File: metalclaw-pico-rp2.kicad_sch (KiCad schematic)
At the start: 114 parts, among them J1 USB_C_Receptacle_USB2.0_14P, J2 Conn_02x05_Odd_Even, SW1 SW_Push, SW2 SW_Push, U1 XC6220B331MR, U2 RP2354B, U3 APS6404L-3SQRx-SN, Y1 XRCGB40M000F1S2FR0

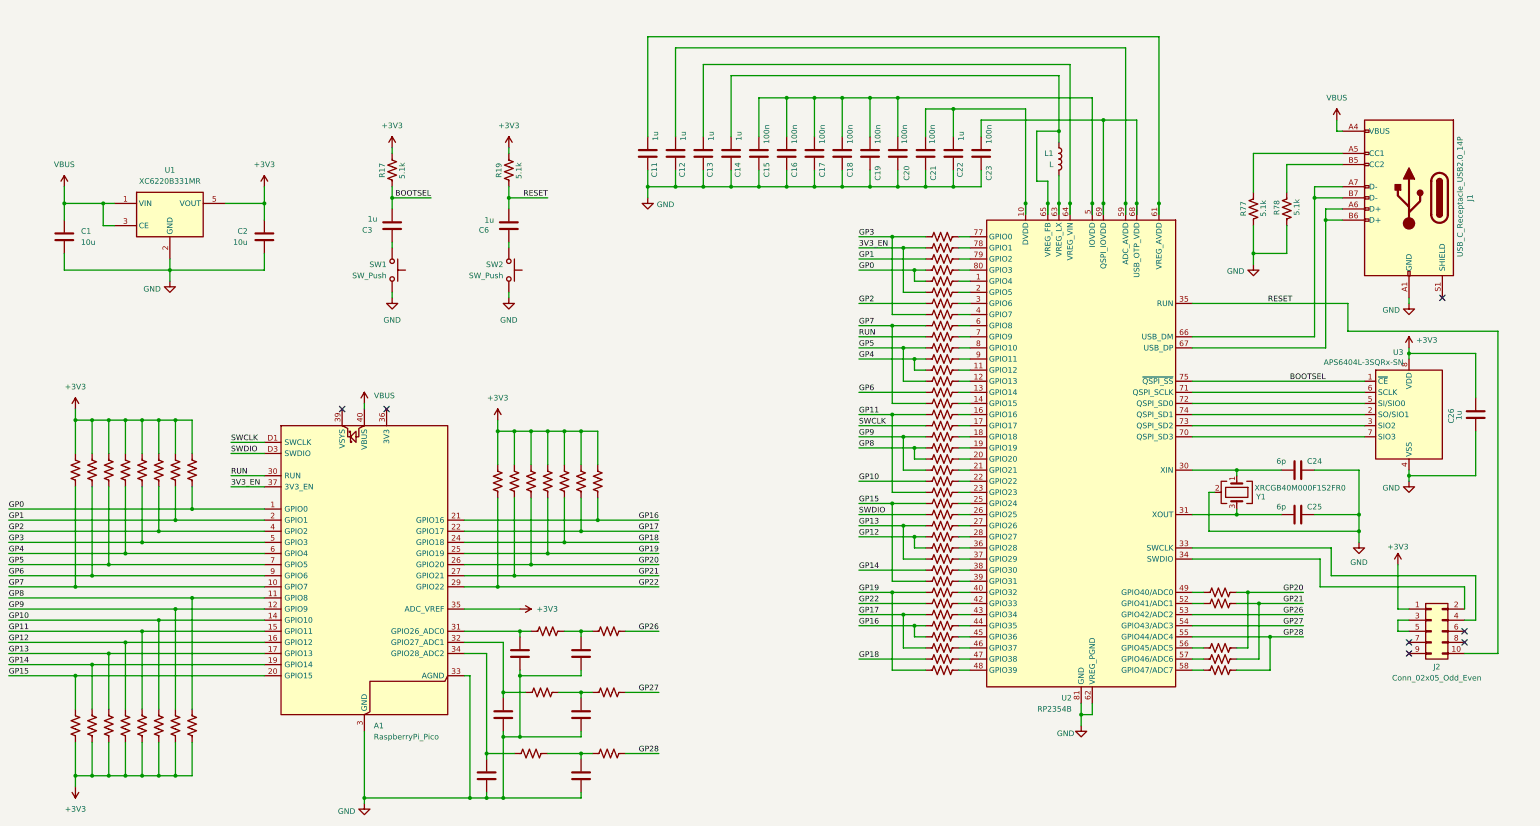
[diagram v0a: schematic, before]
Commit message: Fix all ERC errors and warnings
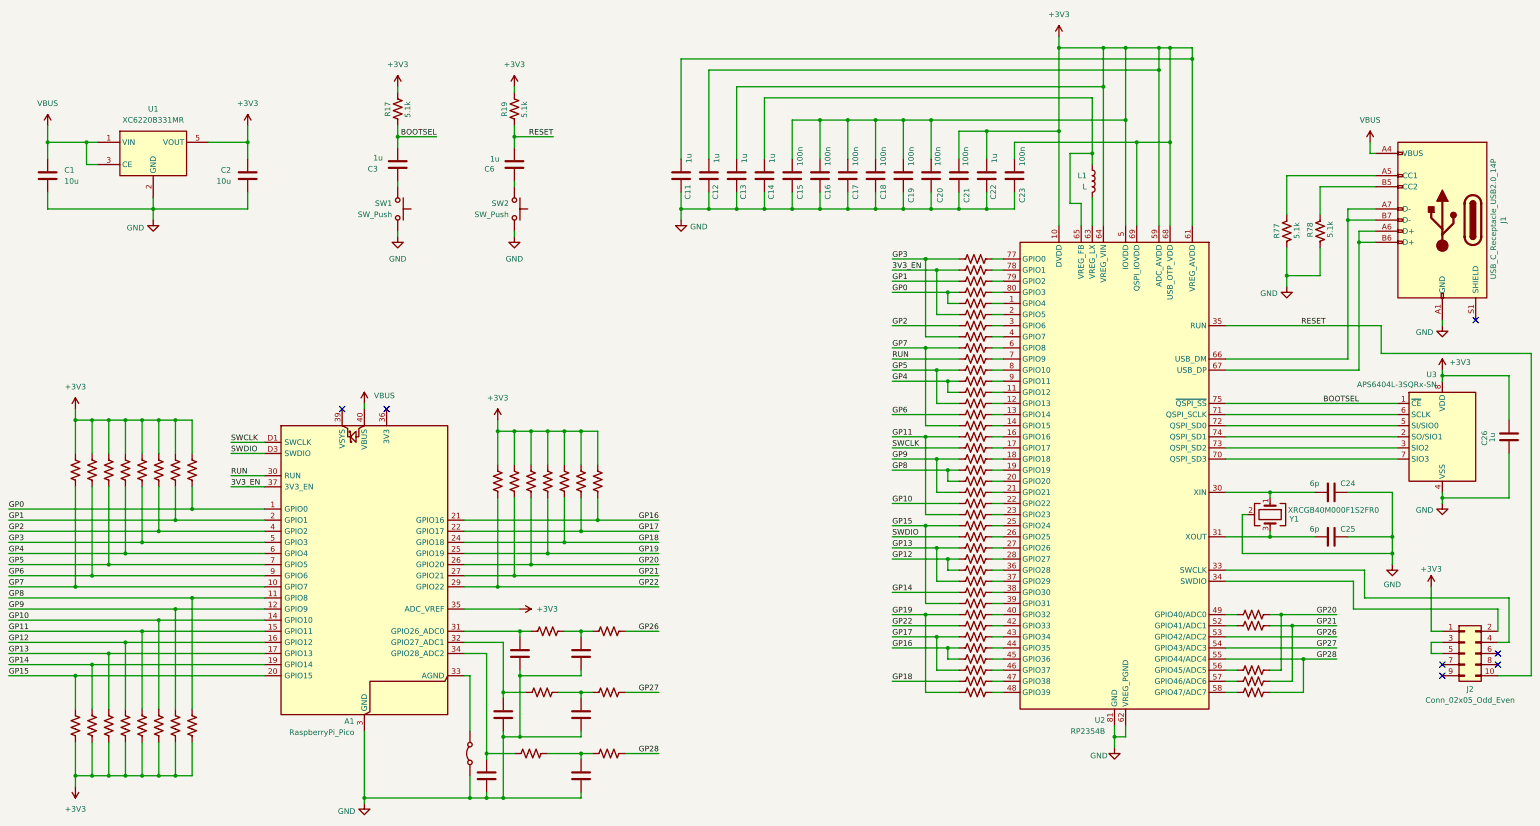
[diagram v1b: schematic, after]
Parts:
- added JP1: Jumper_2_Bridged, Jumper:SolderJumper-2_P1.3mm_Bridged2Bar_Pad1.0x1.5mm, symbol Jumper:Jumper_2_Bridged
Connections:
- net +3V3: now also C11.2, C12.2, C13.2, C15.2, C16.2, C17.2, C18.2, C19.2, C20.2, C21.2, C22.2, C23.2, U2.10 (DVDD), U2.15 (IOVDD), U2.24 (IOVDD), U2.29 (IOVDD), U2.32 (DVDD), U2.41 (IOVDD), U2.5 (IOVDD), U2.50 (IOVDD), U2.51 (DVDD), U2.59 (ADC_AVDD), U2.60 (IOVDD), U2.61 (VREG_AVDD), U2.64 (VREG_VIN), U2.68 (USB_OTP_VDD), U2.69 (QSPI_IOVDD), U2.76 (IOVDD)
- net GND: now also JP1.1 (A); no longer A1.33 (AGND)
- new net: A1.33 (AGND), JP1.2 (B)
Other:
- moved on the sheet: C1, C11, C12, C13, C14, C15, C16, C17, C18, C19, C2, C20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

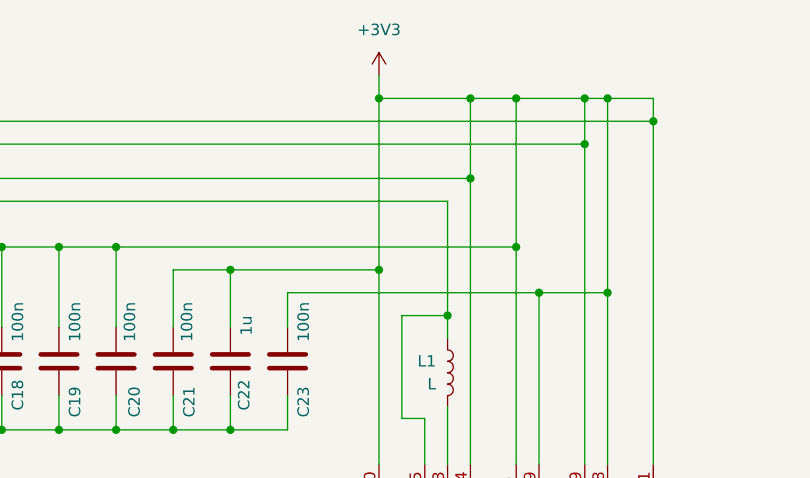
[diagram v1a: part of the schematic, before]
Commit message: Fix DVDD connections
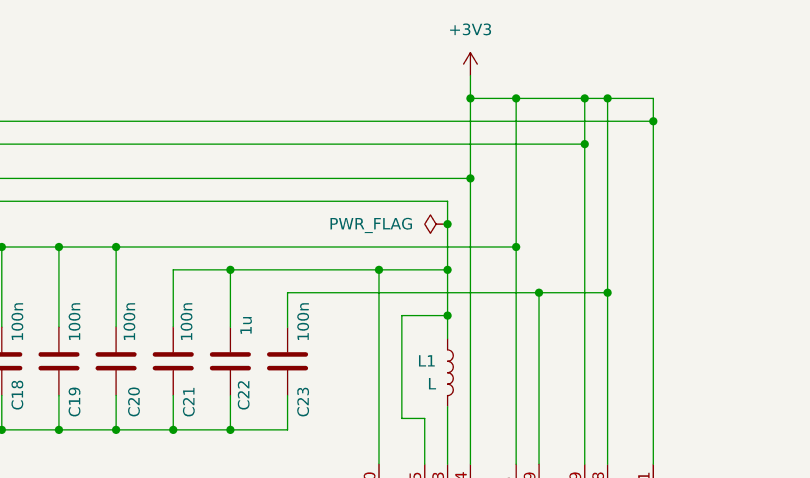
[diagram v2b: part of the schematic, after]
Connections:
- net +3V3: no longer C21.2, C22.2, U2.10 (DVDD), U2.32 (DVDD), U2.51 (DVDD)
- net at C14.2, L1.1, U2.65 (VREG_FB): now also C21.2, C22.2, U2.10 (DVDD), U2.32 (DVDD), U2.51 (DVDD)
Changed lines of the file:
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@@
 	)
 	(junction
+		(at 290.83 68.58)
+		(diameter 0)
+		(color 0 0 0 0)
+	)
+	(junction
 		(at 170.18 137.16)
 		(diameter 0)
@@
 	)
 	(junction
-		(at 283.21 68.58)
-		(diameter 0)
-		(color 0 0 0 0)
-	)
-	(junction
 		(at 209.55 86.36)
 		(diameter 0)
@@
 	)
 	(junction
+		(at 290.83 63.5)
+		(diameter 0)
+		(color 0 0 0 0)
+	)
+	(junction
 		(at 162.56 137.16)
 		(diameter 0)
@@
 	)
 	(junction
-		(at 283.21 49.53)
-		(diameter 0)
-		(color 0 0 0 0)
-	)
-	(junction
 		(at 62.23 215.9)
 		(diameter 0)
@@
 	)
 	(junction
+		(at 283.21 68.58)
+		(diameter 0)
+		(color 0 0 0 0)
+	)
+	(junction
 		(at 81.28 215.9)
 		(diameter 0)
@@
 	(wire
 		(pts
+			(xy 283.21 68.58) (xy 290.83 68.58)
+		)
+		(stroke
+			(width 0)
+			(type default)
+		)
+	)
+	(wire
+		(pts
 			(xy 152.4 210.82) (xy 158.75 210.82)
 		)
@@
 	(wire
 		(pts
-			(xy 283.21 46.99) (xy 283.21 49.53)
+			(xy 293.37 46.99) (xy 293.37 49.53)
 		)
 		(stroke
@@
 	(wire
 		(pts
+			(xy 290.83 63.5) (xy 290.83 68.58)
+		)
+		(stroke
+			(width 0)
+			(type default)
+		)
+	)
+	(wire
+		(pts
 			(xy 323.85 181.61) (xy 321.31 181.61)
 		)
@@
 	(wire
 		(pts
-			(xy 290.83 60.96) (xy 290.83 73.66)
+			(xy 290.83 60.96) (xy 290.83 63.5)
 		)
 		(stroke
@@
 	(wire
 		(pts
-			(xy 293.37 49.53) (xy 283.21 49.53)
+			(xy 290.83 68.58) (xy 290.83 73.66)
 		)
 		(stroke
@@
 	(wire
 		(pts
-			(xy 283.21 49.53) (xy 283.21 68.58)
-		)
-		(stroke
-			(width 0)
-			(type default)
-		)
-	)
-	(wire
-		(pts
 			(xy 52.07 86.36) (xy 76.2 86.36)
 		)
@@
 	)
 	(symbol
+		(lib_id "power:PWR_FLAG")
+		(at 290.83 63.5 90)
+		(unit 1)
+		(exclude_from_sim no)
+		(in_bom yes)
+		(on_board yes)
+		(dnp no)
+		(fields_autoplaced yes)
+		(property "Reference" "#FLG01"
+			(at 288.925 63.5 0)
+			(effects
+				(font
+					(size 1.27 1.27)
+				)
+				(hide yes)
+			)
+		)
+		(property "Value" "PWR_FLAG"
+			(at 287.02 63.4999 90)
+			(effects
+				(font
+					(size 1.27 1.27)
+				)
+				(justify left)
+			)
+		)
+		(property "Footprint" ""
+			(at 290.83 63.5 0)
+			(effects
+				(font
+					(size 1.27 1.27)
+				)
+				(hide yes)
+			)
+		)
+		(property "Datasheet" "~"
+			(at 290.83 63.5 0)
+			(effects
+				(font
+					(size 1.27 1.27)
+				)
+				(hide yes)
+			)
+		)
+		(property "Description" "Special symbol for telling ERC where power comes from"
+			(at 290.83 63.5 0)
+			(effects
+				(font
+					(size 1.27 1.27)
+				)
+				(hide yes)
+			)
+		)
+		(pin "1"
+		)
+		(instances
+			(project ""
+				(path "/c83ebc88-59c8-491c-acdb-d3cfac2d55f0"
+					(reference "#FLG01")
+					(unit 1)
+				)
+			)
+		)
+	)
+	(symbol
 		(lib_id "Device:C")
 		(at 152.4 215.9 0)
@@
 	(symbol
 		(lib_id "power:+3V3")
-		(at 283.21 46.99 0)
+		(at 293.37 46.99 0)
 		(unit 1)
 		(exclude_from_sim no)
@@
 		(fields_autoplaced yes)
 		(property "Reference" "#PWR023"
-			(at 283.21 50.8 0)
+			(at 293.37 50.8 0)
 			(effects
 				(font
@@
 		)
 		(property "Value" "+3V3"
-			(at 283.21 41.91 0)
+			(at 293.37 41.91 0)
 			(effects
 				(font
@@
 		)
 		(property "Footprint" ""
-			(at 283.21 46.99 0)
+			(at 293.37 46.99 0)
 			(effects
 				(font
@@
 		)
 		(property "Datasheet" ""
-			(at 283.21 46.99 0)
+			(at 293.37 46.99 0)
 			(effects
 				(font
@@
 		)
 		(property "Description" "Power symbol creates a global label with name \"+3V3\""
-			(at 283.21 46.99 0)
+			(at 293.37 46.99 0)
 			(effects
 				(font

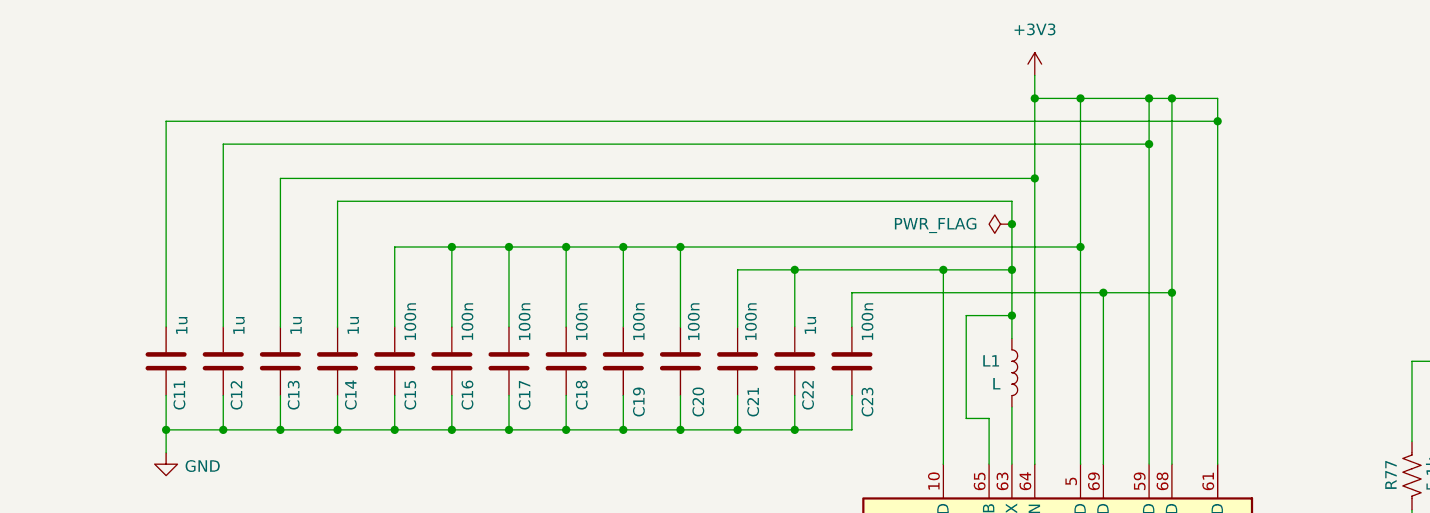
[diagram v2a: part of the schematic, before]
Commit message: Fix VREG_AVDD connection
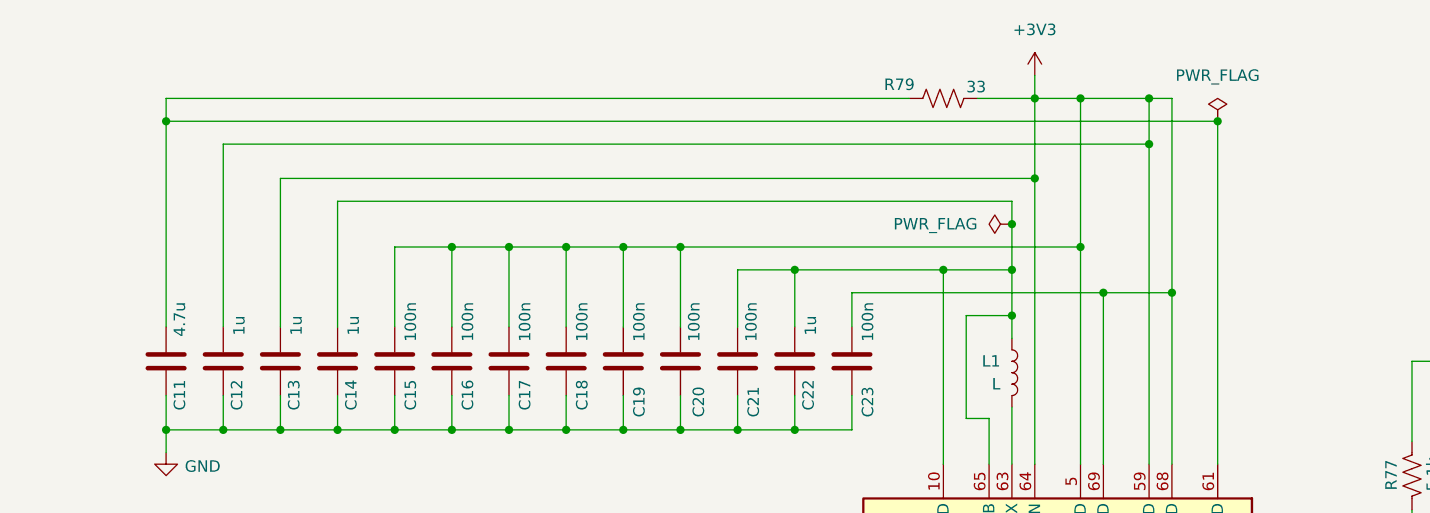
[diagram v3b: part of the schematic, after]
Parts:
- added R79: 33, Resistor_SMD:R_0201_0603Metric, symbol Device:R_US
- C11: value 1u -> 4.7u
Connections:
- net +3V3: now also R79.1; no longer C11.2, U2.61 (VREG_AVDD)
- new net: C11.2, R79.2, U2.61 (VREG_AVDD)
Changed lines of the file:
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@@
 	)
 	(junction
-		(at 313.69 52.07)
-		(diameter 0)
-		(color 0 0 0 0)
-	)
-	(junction
 		(at 234.95 86.36)
 		(diameter 0)
@@
 	)
 	(junction
+		(at 196.85 52.07)
+		(diameter 0)
+		(color 0 0 0 0)
+	)
+	(junction
 		(at 81.28 134.62)
 		(diameter 0)
@@
 	)
 	(junction
-		(at 308.61 49.53)
-		(diameter 0)
-		(color 0 0 0 0)
-	)
-	(junction
 		(at 156.21 196.85)
 		(diameter 0)
@@
 	)
 	(junction
+		(at 313.69 52.07)
+		(diameter 0)
+		(color 0 0 0 0)
+	)
+	(junction
 		(at 166.37 137.16)
 		(diameter 0)
@@
 	(wire
 		(pts
-			(xy 196.85 52.07) (xy 196.85 74.93)
+			(xy 196.85 49.53) (xy 196.85 52.07)
 		)
 		(stroke
@@
 	(wire
 		(pts
+			(xy 196.85 52.07) (xy 313.69 52.07)
+		)
+		(stroke
+			(width 0)
+			(type default)
+		)
+	)
+	(wire
+		(pts
 			(xy 252.73 179.07) (xy 252.73 196.85)
 		)
@@
 	(wire
 		(pts
+			(xy 287.02 49.53) (xy 293.37 49.53)
+		)
+		(stroke
+			(width 0)
+			(type default)
+		)
+	)
+	(wire
+		(pts
 			(xy 321.31 113.03) (xy 356.87 113.03)
 		)
@@
 	(wire
 		(pts
+			(xy 196.85 52.07) (xy 196.85 74.93)
+		)
+		(stroke
+			(width 0)
+			(type default)
+		)
+	)
+	(wire
+		(pts
 			(xy 270.51 148.59) (xy 267.97 148.59)
 		)
@@
 	(wire
 		(pts
+			(xy 279.4 49.53) (xy 196.85 49.53)
+		)
+		(stroke
+			(width 0)
+			(type default)
+		)
+	)
+	(wire
+		(pts
 			(xy 360.68 140.97) (xy 321.31 140.97)
 		)
@@
 	(wire
 		(pts
-			(xy 313.69 49.53) (xy 308.61 49.53)
-		)
-		(stroke
-			(width 0)
-			(type default)
-		)
-	)
-	(wire
-		(pts
 			(xy 336.55 181.61) (xy 331.47 181.61)
 		)
@@
 	(wire
 		(pts
-			(xy 196.85 52.07) (xy 313.69 52.07)
-		)
-		(stroke
-			(width 0)
-			(type default)
-		)
-	)
-	(wire
-		(pts
 			(xy 85.09 154.94) (xy 101.6 154.94)
 		)
@@
 	(wire
 		(pts
-			(xy 313.69 52.07) (xy 313.69 49.53)
-		)
-		(stroke
-			(width 0)
-			(type default)
-		)
-	)
-	(wire
-		(pts
 			(xy 349.25 88.9) (xy 349.25 86.36)
 		)
@@
 			)
 		)
-		(property "Value" "1u"
-			(at 198.628 73.66 90)
+		(property "Value" "4.7u"
+			(at 198.374 72.136 90)
 			(effects
 				(font
@@
 	(symbol
 		(lib_id "Device:R_US")
+		(at 283.21 49.53 270)
+		(unit 1)
+		(exclude_from_sim no)
+		(in_bom yes)
+		(on_board yes)
+		(dnp no)
+		(property "Reference" "R79"
+			(at 276.606 48.006 90)
+			(effects
+				(font
+					(size 1.27 1.27)
+				)
+				(justify left)
+			)
+		)
+		(property "Value" "33"
+			(at 285.75 48.26 90)
+			(effects
+				(font
+					(size 1.27 1.27)
+				)
+				(justify left)
+			)
+		)
+		(property "Footprint" "Resistor_SMD:R_0201_0603Metric"
+			(at 282.956 50.546 90)
+			(effects
+				(font
+					(size 1.27 1.27)
+				)
+				(hide yes)
+			)
+		)
+		(property "Datasheet" "~"
+			(at 283.21 49.53 0)
+			(effects
+				(font
+					(size 1.27 1.27)
+				)
+				(hide yes)
+			)
+		)
+		(property "Description" "Resistor, US symbol"
+			(at 283.21 49.53 0)
+			(effects
+				(font
+					(size 1.27 1.27)
+				)
+				(hide yes)
+			)
+		)
+		(property "Mouser" "71-CRCW02015K10FEDAT "
+			(at 283.21 49.53 90)
+			(effects
+				(font
+					(size 1.27 1.27)
+				)
+				(hide yes)
+			)
+		)
+		(pin "2"
+		)
+		(pin "1"
+		)
+		(instances
+			(project "metalclaw-pico-rp2"
+				(path "/c83ebc88-59c8-491c-acdb-d3cfac2d55f0"
+					(reference "R79")
+					(unit 1)
+				)
+			)
+		)
+	)
+	(symbol
+		(lib_id "Device:R_US")
 		(at 327.66 196.85 90)
 		(unit 1)
@@
 					(unit 1)
 				)
+			)
+		)
+	)
+	(symbol
+		(lib_id "power:PWR_FLAG")
+		(at 313.69 52.07 0)
+		(unit 1)
+		(exclude_from_sim no)
+		(in_bom yes)
+		(on_board yes)
+		(dnp no)
+		(fields_autoplaced yes)
+		(property "Reference" "#FLG02"
+			(at 313.69 50.165 0)
+			(effects
+				(font
+					(size 1.27 1.27)
+				)
+				(hide yes)
+			)
+		)
+		(property "Value" "PWR_FLAG"
+			(at 313.69 46.99 0)
+			(effects
+				(font
+					(size 1.27 1.27)
+				)
+			)
+		)
+		(property "Footprint" ""
+			(at 313.69 52.07 0)
+			(effects
+				(font
+					(size 1.27 1.27)
+				)
+				(hide yes)
+			)
+		)
+		(property "Datasheet" "~"
+			(at 313.69 52.07 0)
+			(effects
+				(font
+					(size 1.27 1.27)
+				)
+				(hide yes)
+			)
+		)
+		(property "Description" "Special symbol for telling ERC where power comes from"
+			(at 313.69 52.07 0)
+			(effects
+				(font
+					(size 1.27 1.27)
+				)
+				(hide yes)
+			)
+		)
+		(pin "1"
+		)
+		(instances
+			(project ""
+				(path "/c83ebc88-59c8-491c-acdb-d3cfac2d55f0"
+					(reference "#FLG02")
+					(unit 1)
+				)

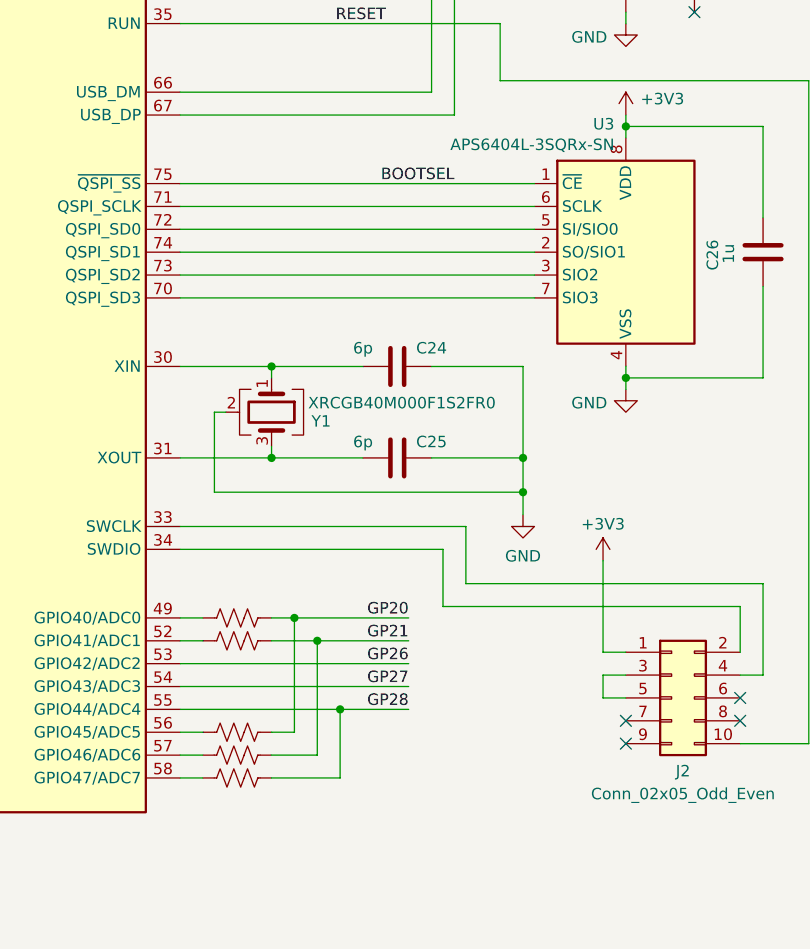
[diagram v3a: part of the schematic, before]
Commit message: Fix PSRAM chip select connection
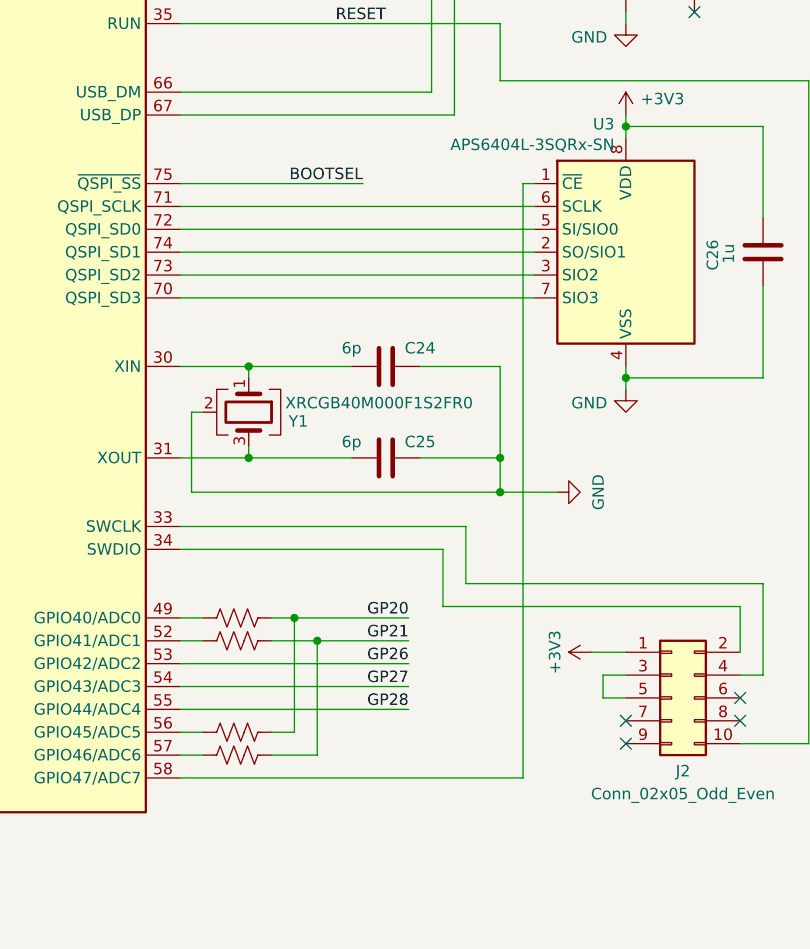
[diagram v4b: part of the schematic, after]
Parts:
- removed R76: 220, Resistor_SMD:R_0201_0603Metric, symbol Device:R_US
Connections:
- net BOOTSEL: no longer U3.1 (~{CE})
- net at U2.58 (GPIO47/ADC7): now also U3.1 (~{CE})
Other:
- moved on the sheet: C24, C25, Y1
